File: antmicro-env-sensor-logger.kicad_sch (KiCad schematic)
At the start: 0 parts

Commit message: [#39176] SCH: Add USB-C input cicuitry, FT4232H-56Q, STM32G474Rx ICs
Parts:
- added C?: C_100n_0402_16V, antmicro-footprints:0603-cap, symbol antmicroCapacitors0603:C_100n_0603
- added C? (x3): C_1u_0603, antmicro-footprints:0603-cap, symbol antmicroCapacitors0603:C_1u_0603
- added C?: C_10n_0402, antmicro-footprints:0603-cap, symbol antmicroCapacitors0603:C_10n_0603
- added C?: C_10u_16V_0603, antmicro-footprints:0603-cap, symbol antmicroCapacitors0603:C_10u_16V_0603
- added D?: TPD2E009, antmicro-footprints:SOT-723, symbol antmicroTVSDiodes:TPD2E009
- added FB?: BLM18PG121SN1D, antmicro-footprints:0603-res, symbol antmicroFerriteBeadsandChips:BLM18PG121SN1D
- added J?: CX90M-16P, antmicro-footprints:USB_C_Receptacle_Hirose_CX90M-16P, symbol antmicroUSBDVIHDMIConnectors:CX90M-16P
- added R? (x2): R_5k1_0603, antmicro-footprints:0603-res, symbol antmicroResistors0603:R_5k1_0603
- added R?: R_470R_0402, antmicro-footprints:0603-res, symbol antmicroResistors0603:R_470R_0603
- added U? (x2): STM32G474Rx, antmicro-footprints:LQFP-64_10x10mm, symbol antmicroMicrocontrollers:STM32G474Rx
- added U?: FT4232H-56Q, antmicro-footprints:QFN-56-1EP_8x8mm_P0.5mm_EP5.5.9x5.9mm, symbol antmicroInterfaceControllers:FT4232H-56Q
- added USB?: LG_L29K-G2J1-24-Z, antmicro-footprints:LED_0603, symbol antmicroLEDIndicationDiscrete:KP-1608ZGC
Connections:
- new net: C?.2, FB?.1, USB?.1
- new net: C?.1, FB?.2, J?.A4 (VBUS), J?.A9 (VBUS), J?.B4 (VBUS), J?.B9 (VBUS)
- new net: R?.2, USB?.2
- new net GND: C?.1, C?.2, D?.3 (GND), J?.A1 (GND), J?.A12 (GND), J?.B1 (GND), J?.B12 (GND), R?.1, R?.1, R?.1
- new net GNDREF: J?.S1 (SHIELD)
- new net USB_CC1: J?.A5 (CC1), R?.2
- new net USB_CC2: J?.B5 (CC2), R?.2
- new net USB_D_N: D?.2 (IO2), J?.A7 (D-), J?.B7 (D-)
- new net USB_D_P: D?.1 (IO1), J?.A6 (D+), J?.B6 (D+)

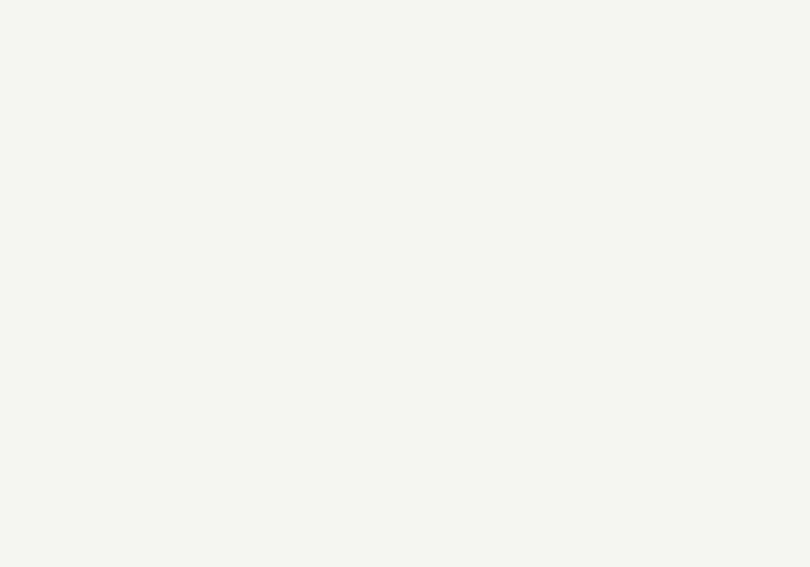
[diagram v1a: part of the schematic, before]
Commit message: [#39176] Added Fujitsu I²C 128KB FeRAM memory
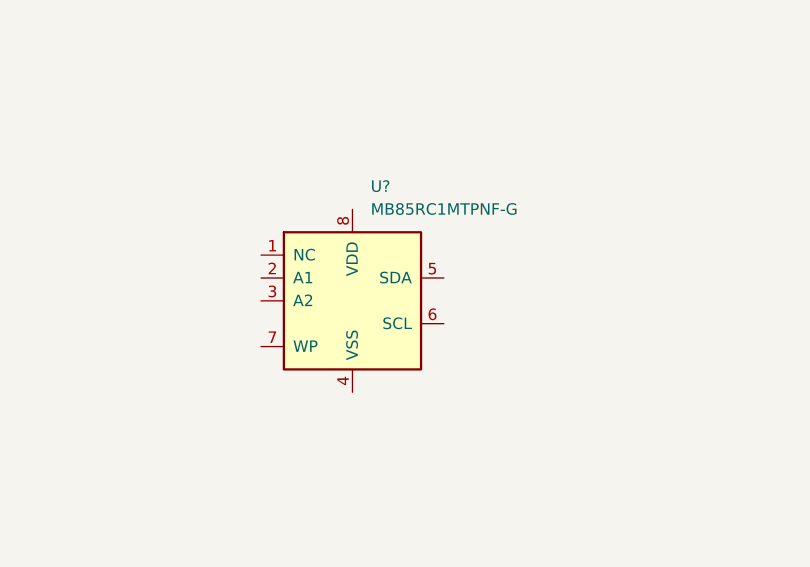
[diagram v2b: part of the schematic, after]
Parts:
- added U?: MB85RC1MTPNF-G, antmicro-footprints:SOIC-8_W3.9mm, symbol antmicroMemory:MB85RC1MTPNF-G
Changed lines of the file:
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@@
     (pin "1")
+  )
+  (symbol (lib_id "antmicroMemory:MB85RC1MTPNF-G") (at 264.16 165.1 0) (unit 1)
+    (in_bom yes) (on_board yes) (fields_autoplaced)
+    (property "Reference" "U?" (id 0) (at 266.1794 152.4 0)
+      (effects (font (size 1.27 1.27)) (justify left))
+    )
+    (property "Value" "MB85RC1MTPNF-G" (id 1) (at 266.1794 154.94 0)
+      (effects (font (size 1.27 1.27)) (justify left))
+    )
+    (property "Footprint" "antmicro-footprints:SOIC-8_W3.9mm" (id 2) (at 266.7 154.94 0)
+      (effects (font (size 1.524 1.524)) (justify left) hide)
+    )
+    (property "Datasheet" "https://www.fujitsu.com/jp/group/fsm/en/documents/products/feram/lineup/MB85RC1MT-DS501-00027-5v0-E.pdf" (id 3) (at 266.7 152.4 0)
+      (effects (font (size 1.524 1.524)) (justify left) hide)
+    )
+    (property "MPN" "MB85RC1MTPNF-G-JNERE1" (id 4) (at 266.7 149.86 0)
+      (effects (font (size 1.524 1.524)) (justify left) hide)
+    )
+    (property "Manufacturer" "Fujitsu Semiconductor Ltd" (id 5) (at 266.7 147.32 0)
+      (effects (font (size 1.524 1.524)) (justify left) hide)
+    )
+    (pin "1")
+    (pin "2")
+    (pin "3")
+    (pin "4")
+    (pin "5")
+    (pin "6")
+    (pin "7")
+    (pin "8")
   )
   (symbol (lib_id "antmicroResistors0603:R_470R_0603") (at 124.46 62.865 90) (unit 1)
@@
       (reference "U?") (unit 1) (value "FT4232H-56Q") (footprint "antmicro-footprints:QFN-56-1EP_8x8mm_P0.5mm_EP5.5.9x5.9mm")
     )
+    (path "/c5c012ff-1a2c-4ebc-9da4-4310c7a4116c"
+      (reference "U?") (unit 1) (value "MB85RC1MTPNF-G") (footprint "antmicro-footprints:SOIC-8_W3.9mm")
+    )
     (path "/03650765-a79b-43d8-84e0-1b3e68d5acee"
